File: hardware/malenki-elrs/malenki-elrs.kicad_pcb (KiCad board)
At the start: 4 copper layers, 19 x 32 mm, 56 parts, among them J1 Conn_01x02_Male-Connector, J2 PROG Header, J3 Weapons, J4 Conn_01x02_Male-Connector, J5 Conn_01x02_Male-Connector, J6 Conn_01x02_Male-Connector, U1 SPX3819M5-L-3-3, U2 ESP32-C3FH4, U3 SX1280IMLTRT, U4 DRV8837DSGR, U5 DRV8837DSGR, U6 DRV8837DSGR, Y1 ECS-400-10-37B2-CKY-TR, Y2 CRYSTAL 52MHz 10pF SMD

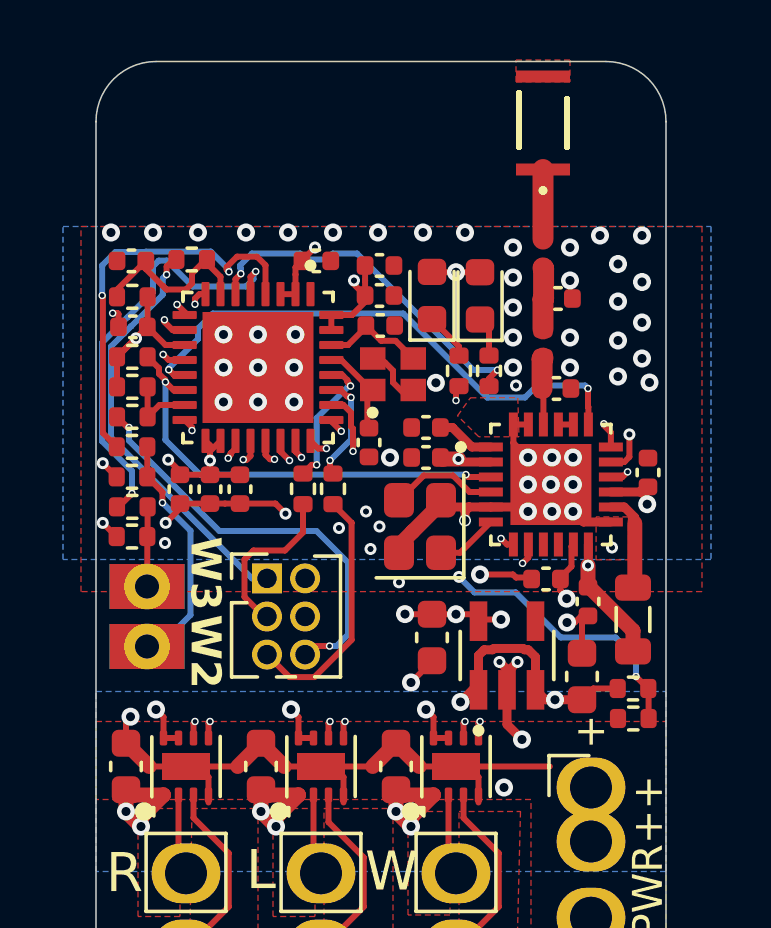
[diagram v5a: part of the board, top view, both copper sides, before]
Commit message: Changed microcontroller and completed schematic
Changed micro controller to the esp32-s3FN8, for more available pins.
Complete schematic.
Changed to pcb antenna.
Completed initial placement of all components on PCB.
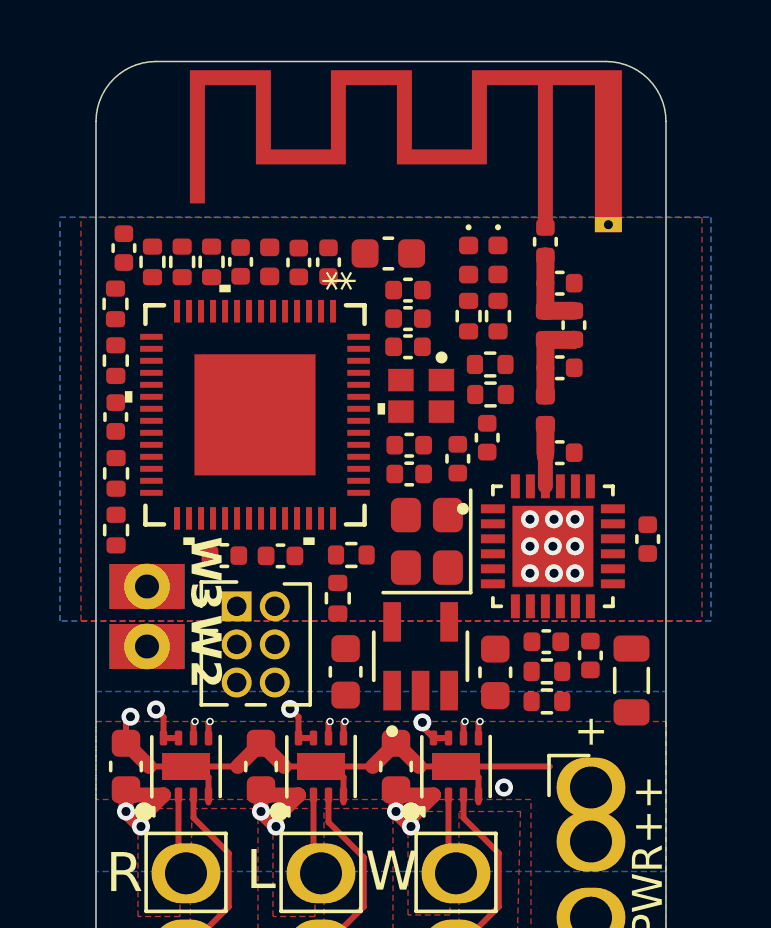
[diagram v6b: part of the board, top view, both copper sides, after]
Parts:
- removed ANT1: ANT3216LL00R2400A, malenki-nano:ANT3216LL00R2400A
- removed U2: ESP32-C3FH4, malenki-nano:QFN50P500X500X90-33N
- added AE1: ~, malenki-nano:malenki_antenna, F.Cu at (103.0, 54.9)
- added C11: 100nF, Capacitor_SMD:C_0402_1005Metric, F.Cu at (95.8, 56.2)
- added C12: 1uF, Capacitor_SMD:C_0402_1005Metric, F.Cu at (94.8, 56.2)
- added C14: 10uF, Capacitor_SMD:C_0603_1608Metric, F.Cu at (97.7, 55.9)
- added C28: 1.2pF, Capacitor_SMD:C_0402_1005Metric, F.Cu at (103.5, 56.9)
- added C29: 0.5pF, Capacitor_SMD:C_0402_1005Metric, F.Cu at (103.9, 58.3)
- added C30: 100pF, Capacitor_SMD:C_0402_1005Metric, F.Cu at (103.0, 55.5)
- added L3: 2.5nH, Inductor_SMD:L_0402_1005Metric, F.Cu at (103.0, 58.3)
- added L4: 2nH, Inductor_SMD:L_0402_1005Metric, F.Cu at (93.8, 56.2)
- added U7: ESP32-S3FN8, malenki-nano:QFN56_7X7_EXP, F.Cu at (93.3, 61.3)
- C20: value 10pF -> 0.8pF
- C23: value 10pF -> 1.2pF
- C6: value 100nF -> 10nF
- D1, D2: footprint LED_SMD:LED_0603_1608Metric -> LED_SMD:LED_0402_1005Metric
- L2: value 3.9nH -> 3nH
- moved R13 9.20 mm to (96.5, 66.0)
- moved R14 9.14 mm to (96.1, 67.4), turned to -90 degrees
- moved R2 7.77 mm to (88.7, 57.6), turned to 90 degrees
- moved C7 7.75 mm to (98.4, 63.2)
- moved C10 7.64 mm to (92.8, 56.2), turned to 90 degrees
- moved R12 7.00 mm to (101.2, 60.6), turned to 180 degrees
- moved R11 6.68 mm to (101.1, 59.6), turned to 180 degrees
- moved R4 4.91 mm to (88.7, 59.5), turned to -90 degrees
- moved R15 4.12 mm to (91.9, 56.2), turned to -90 degrees
- moved C3 4.11 mm to (98.4, 62.3)
- moved C2 3.44 mm to (98.4, 59.0), turned to 180 degrees
- moved R8 3.28 mm to (103.0, 69.8)
- moved C5 3.10 mm to (96.3, 69.8)
- moved C13 3.06 mm to (88.7, 61.4), turned to -90 degrees
- moved R7 2.90 mm to (103.0, 70.8)
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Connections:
- net ESP_NRESET renamed RADIO_NRESET
- net Net-(U2-XTAL_N) renamed XTAL_P
- net Net-(U2-XTAL_P) renamed XTAL_N
- C10 pad 1: VLOGIC -> Net-(C10-Pad1)
- D1 pad 1: Net-(D1-K) -> GND
- D1 pad 2: VLOGIC -> Net-(D1-A)
- D2 pad 1: Net-(D2-K) -> GND
- D2 pad 2: VLOGIC -> Net-(D2-A)
- R10 pad 1: Net-(D2-K) -> Net-(D2-A)
- R9 pad 1: Net-(D1-K) -> Net-(D1-A)
- U3 pad 16: ESP_MISO -> RADIO_MISO
- U3 pad 17: ESP_MOSI -> RADIO_MOSI
- U3 pad 18: ESP_SCK -> RADIO_SCK
- U3 pad 19: ESP_NSS -> RADIO_NSS
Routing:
- net GND: track 49.1 -> 22.1 mm, vias 70 -> 11
- net VLOGIC: track 30.4 -> 4.32 mm, vias 14 -> 3
- net MOTOR1F: track 22.3 -> 0.57 mm, vias 2 -> 1
- net MOTOR1R: track 21.7 -> 0.57 mm, vias 2 -> 1
- net ESP_SCK: track 21.0 -> 0.00 mm, vias 2 -> 0
- net ESP_MOSI: track 21.0 -> 0.00 mm, vias 2 -> 0
- net ESP_MISO: track 18.8 -> 0.00 mm, vias 2 -> 0
- net ESP_NSS: track 18.2 -> 0.00 mm, vias 2 -> 0
- net VSENSE: track 16.9 -> 0.00 mm, vias 3 -> 0
- net BUSY: track 15.7 -> 0.00 mm, vias 2 -> 0
- net RADIO_NRESET: track 15.1 -> 0.00 mm, vias 2 -> 0
- net DIO1: track 14.7 -> 0.00 mm, vias 2 -> 0
- net /W3: track 14.4 -> 0.00 mm, vias 2 -> 0
- net ESPIO0: track 14.1 -> 0.00 mm, vias 2 -> 0
- net ESP_EN: track 14.0 -> 0.00 mm, vias 1 -> 0
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- removed copper zone on F.Cu, net unconnected-(ANT1-Pad2)
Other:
- board text removed: "@markxr 2023"

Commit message: Changed component parts to match JLCPCB basic parts
Saving assembly cost by changing all possible components to JLCPCB basic part, and reducing number of separate components where possible. Started trace placement
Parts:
- C29: value 0.5pF -> 0.8pF
- L3: value 2.5nH -> 3nH
- R10, R9: value 1k -> 470
- moved C21 0.64 mm to (104.5, 69.9)
- moved C22 0.05 mm to (106.4, 65.4)
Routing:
- net GND: track 22.1 -> 34.0 mm, vias 11 -> 34
- net VBAT: track 12.3 -> 18.7 mm, vias 6 -> 8
- net VLOGIC: track 4.32 -> 8.78 mm, vias 3 -> 5
- net Net-(U3-DCC_FB): track 0.00 -> 4.30 mm
- net Net-(U3-DCC_SW): track 0.00 -> 3.55 mm
- net RADIO_MOSI: track 0.00 -> 1.12 mm, vias 0 -> 1
- net VSENSE: track 0.00 -> 1.00 mm
- net RADIO_MISO: track 0.00 -> 0.68 mm, vias 0 -> 1
- net MOTOR3R: track 0.57 -> 0.00 mm, vias 1 -> 0
- net MOTOR3F: track 0.57 -> 0.00 mm, vias 1 -> 0
- net MOTOR2R: track 0.57 -> 0.00 mm, vias 1 -> 0
- net MOTOR2F: track 0.57 -> 0.00 mm, vias 1 -> 0
- net MOTOR1R: track 0.57 -> 0.00 mm, vias 1 -> 0
- net MOTOR1F: track 0.57 -> 0.00 mm, vias 1 -> 0
- net RADIO_SCK: track 0.00 -> 0.55 mm, vias 0 -> 1
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
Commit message: Completed trace placement
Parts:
- removed D1: LED Blue, LED_SMD:LED_0402_1005Metric
- removed R9: 470, Resistor_SMD:R_0402_1005Metric
- moved L4 0.70 mm to (94.5, 56.1)
- moved C12 0.69 mm to (95.4, 56.1), turned to 90 degrees
- moved C11 0.64 mm to (96.4, 56.1), turned to 90 degrees
- moved C14 0.60 mm to (98.3, 55.9)
- moved R13 0.54 mm to (97.0, 66.1), turned to -90 degrees
- moved C10 0.39 mm to (93.2, 56.1)
- moved R5 0.33 mm to (89.6, 56.4)
- moved R15 0.30 mm to (91.6, 56.1)
- moved R6 0.30 mm to (90.6, 56.2)
- moved C4 0.30 mm to (88.6, 55.7)
- moved C9 0.27 mm to (93.9, 66.0)
- moved C15 0.27 mm to (92.0, 66.0)
- moved D2 0.07 mm to (100.3, 56.1)
- moved R10 0.07 mm to (100.3, 58.0)
- moved C13 0.06 mm to (88.6, 61.4)
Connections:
- U7 pad 18: BLINKY -> unconnected-(U7-GPIO13-Pad18)
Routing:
- net VSENSE: track 1.00 -> 38.8 mm, vias 0 -> 2
- net BUSY: track 0.00 -> 25.8 mm, vias 0 -> 2
- net RADIO_SCK: track 0.55 -> 25.1 mm, vias 1 -> 2
- net RADIO_MOSI: track 1.12 -> 23.0 mm, vias 1 -> 2
- net DIO1: track 0.00 -> 21.6 mm, vias 0 -> 3
- net MOTOR1F: track 0.00 -> 21.5 mm, vias 0 -> 2
- net MOTOR1R: track 0.00 -> 21.3 mm, vias 0 -> 2
- net RADIO_NRESET: track 0.00 -> 20.8 mm, vias 0 -> 3
- net U0RXD: track 0.00 -> 20.5 mm, vias 0 -> 1
- net RADIO_MISO: track 0.68 -> 21.0 mm, vias 1 -> 2
- net MOTOR2F: track 0.00 -> 20.1 mm, vias 0 -> 2
- net Net-(U7-GPIO0): track 0.00 -> 19.7 mm, vias 0 -> 3
- net U0TXD: track 0.00 -> 19.2 mm, vias 0 -> 1
- net RADIO_NSS: track 0.54 -> 19.1 mm, vias 1 -> 2
- net VLOGIC: track 8.78 -> 27.1 mm, vias 5 -> 13
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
